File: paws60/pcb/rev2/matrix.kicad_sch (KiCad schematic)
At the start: 139 parts

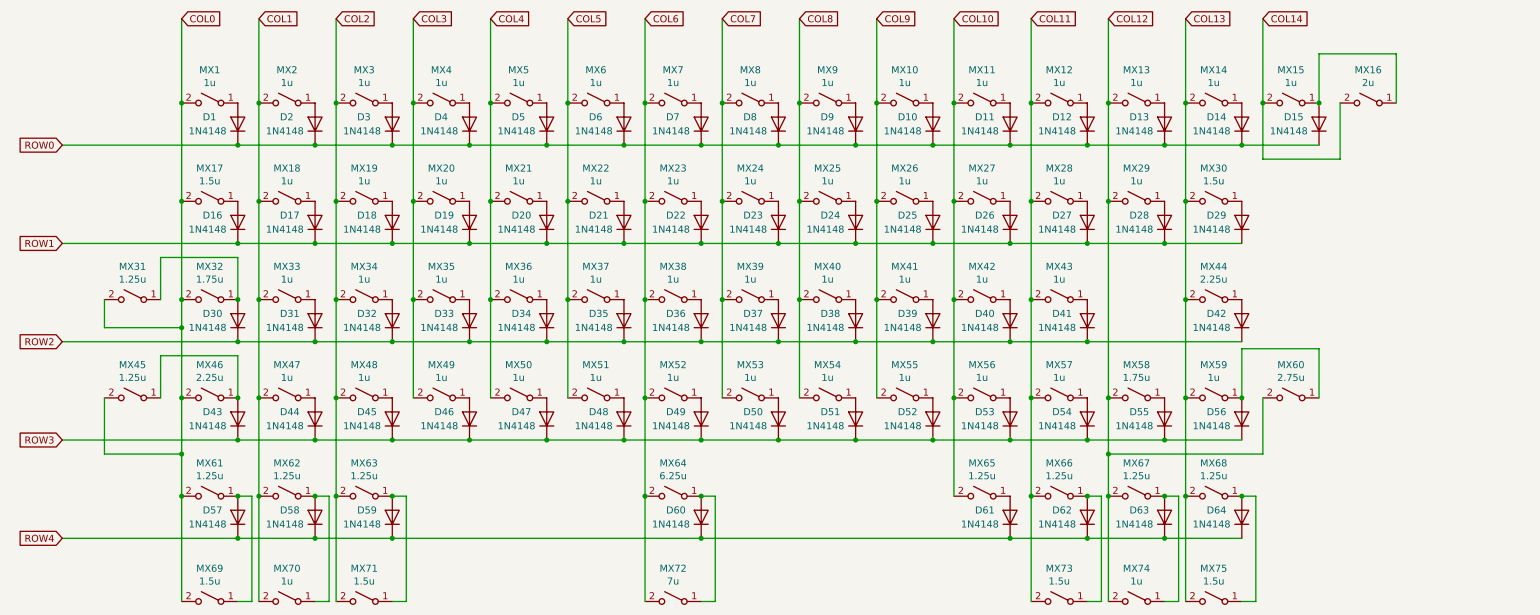
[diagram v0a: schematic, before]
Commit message: Update paws60 hotswap socket footprint and lazulipad
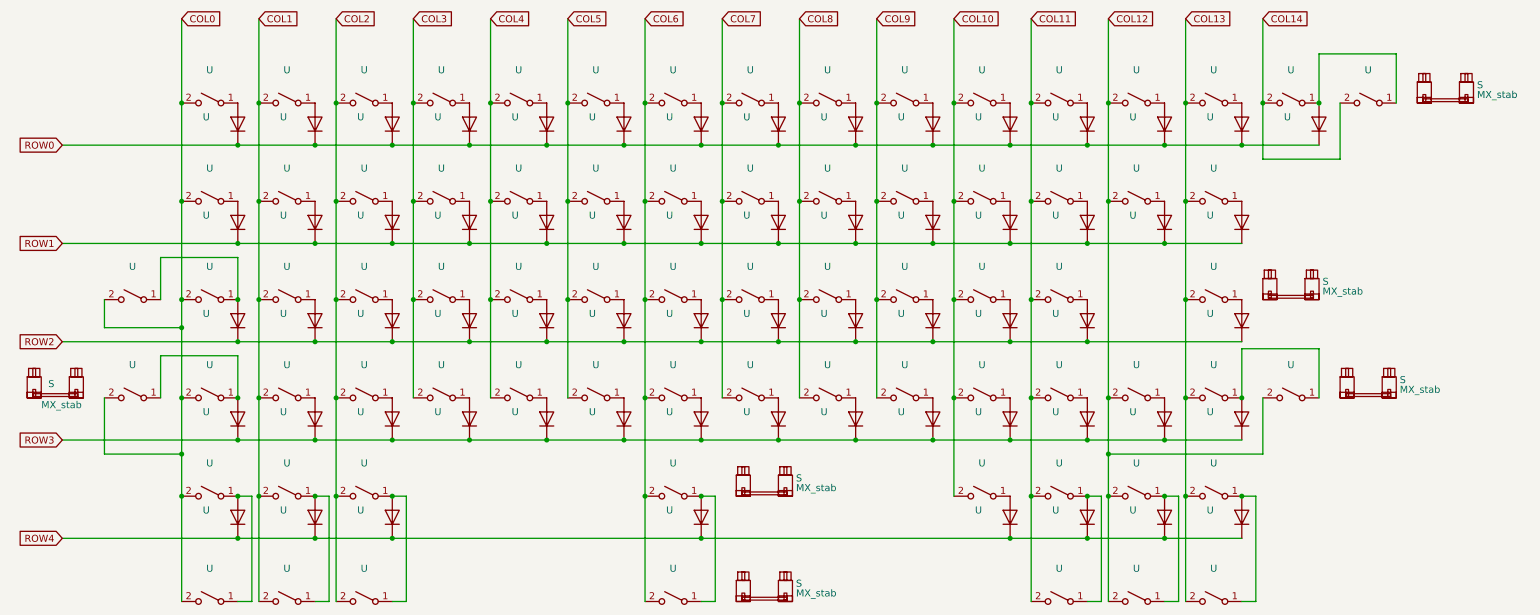
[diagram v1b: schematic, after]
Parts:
- added S (x6): MX_stab, marbastlib-mx:STAB_MX_P_6.25u, symbol marbastlib-mx:MX_stab
- U: renamed from MX60; value 2.75u -> (none); footprint MX_Only:MXOnly-2.75U-Hotswap -> (none)
- U: renamed from MX74; value 1u -> (none); footprint MX_Only:MXOnly-1U-Hotswap -> (none)
- U: renamed from MX75; value 1.5u -> (none); footprint MX_Only:MXOnly-1.5U-Hotswap -> (none)
- U: renamed from MX72; value 7u -> (none); footprint MX_Only:MXOnly-7U-Hotswap -> (none)
- U: renamed from MX69; value 1.5u -> (none); footprint MX_Only:MXOnly-1.5U-Hotswap -> (none)
- U: renamed from MX70; value 1u -> (none); footprint MX_Only:MXOnly-1U-Hotswap -> (none)
- U: renamed from MX71; value 1.5u -> (none); footprint MX_Only:MXOnly-1.5U-Hotswap -> (none)
- U: renamed from MX17; value 1.5u -> (none); footprint MX_Only:MXOnly-1.5U-Hotswap -> (none)
- U: renamed from MX5; value 1u -> (none); footprint MX_Only:MXOnly-1U-Hotswap -> (none)
- U: renamed from MX31; value 1.25u -> (none); footprint MX_Only:MXOnly-1.25U-Hotswap -> (none)
- U: renamed from MX16; value 2u -> (none); footprint MX_Only:MXOnly-2U-Hotswap -> (none)
- U: renamed from MX73; value 1.5u -> (none); footprint MX_Only:MXOnly-1.5U-Hotswap -> (none)
- U: renamed from MX32; value 1.75u -> (none); footprint MX_Only:MXOnly-1.75U-Hotswap -> (none)
- U: renamed from MX46; value 2.25u -> (none); footprint MX_Only:MXOnly-2.25U-Hotswap -> (none)
- U: renamed from D64; value 1N4148 -> (none); footprint Diode_SMD:D_SOD-123 -> (none)
- U: renamed from MX68; value 1.25u -> (none); footprint MX_Only:MXOnly-1.25U-Hotswap -> (none)
- U: renamed from D63; value 1N4148 -> (none); footprint Diode_SMD:D_SOD-123 -> (none)
- U: renamed from MX67; value 1.25u -> (none); footprint MX_Only:MXOnly-1.25U-Hotswap -> (none)
- U: renamed from D62; value 1N4148 -> (none); footprint Diode_SMD:D_SOD-123 -> (none)
- U: renamed from MX66; value 1.25u -> (none); footprint MX_Only:MXOnly-1.25U-Hotswap -> (none)
- U: renamed from D61; value 1N4148 -> (none); footprint Diode_SMD:D_SOD-123 -> (none)
- U: renamed from MX65; value 1.25u -> (none); footprint MX_Only:MXOnly-1.25U-Hotswap -> (none)
- U: renamed from D60; value 1N4148 -> (none); footprint Diode_SMD:D_SOD-123 -> (none)
- U: renamed from MX64; value 6.25u -> (none); footprint MX_Only:MXOnly-6.25U-Hotswap-ReversedStabilizers -> (none)
- U: renamed from D59; value 1N4148 -> (none); footprint Diode_SMD:D_SOD-123 -> (none)
- U: renamed from MX63; value 1.25u -> (none); footprint MX_Only:MXOnly-1.25U-Hotswap -> (none)
- U: renamed from D58; value 1N4148 -> (none); footprint Diode_SMD:D_SOD-123 -> (none)
- U: renamed from MX62; value 1.25u -> (none); footprint MX_Only:MXOnly-1.25U-Hotswap -> (none)
- U: renamed from D57; value 1N4148 -> (none); footprint Diode_SMD:D_SOD-123 -> (none)
- U: renamed from MX61; value 1.25u -> (none); footprint MX_Only:MXOnly-1.25U-Hotswap -> (none)
- U: renamed from D56; value 1N4148 -> (none); footprint Diode_SMD:D_SOD-123 -> (none)
- U: renamed from MX59; value 1u -> (none); footprint MX_Only:MXOnly-1U-Hotswap -> (none)
- U: renamed from D55; value 1N4148 -> (none); footprint Diode_SMD:D_SOD-123 -> (none)
- U: renamed from MX58; value 1.75u -> (none); footprint MX_Only:MXOnly-1.75U-Hotswap -> (none)
- U: renamed from D54; value 1N4148 -> (none); footprint Diode_SMD:D_SOD-123 -> (none)
- U: renamed from MX57; value 1u -> (none); footprint MX_Only:MXOnly-1U-Hotswap -> (none)
- U: renamed from D53; value 1N4148 -> (none); footprint Diode_SMD:D_SOD-123 -> (none)
- U: renamed from MX56; value 1u -> (none); footprint MX_Only:MXOnly-1U-Hotswap -> (none)
- U: renamed from D52; value 1N4148 -> (none); footprint Diode_SMD:D_SOD-123 -> (none)
- U: renamed from MX55; value 1u -> (none); footprint MX_Only:MXOnly-1U-Hotswap -> (none)
- U: renamed from D51; value 1N4148 -> (none); footprint Diode_SMD:D_SOD-123 -> (none)
- U: renamed from MX54; value 1u -> (none); footprint MX_Only:MXOnly-1U-Hotswap -> (none)
- U: renamed from D50; value 1N4148 -> (none); footprint Diode_SMD:D_SOD-123 -> (none)
- U: renamed from MX53; value 1u -> (none); footprint MX_Only:MXOnly-1U-Hotswap -> (none)
- U: renamed from D49; value 1N4148 -> (none); footprint Diode_SMD:D_SOD-123 -> (none)
- U: renamed from MX52; value 1u -> (none); footprint MX_Only:MXOnly-1U-Hotswap -> (none)
- U: renamed from D48; value 1N4148 -> (none); footprint Diode_SMD:D_SOD-123 -> (none)
- U: renamed from MX51; value 1u -> (none); footprint MX_Only:MXOnly-1U-Hotswap -> (none)
- U: renamed from D47; value 1N4148 -> (none); footprint Diode_SMD:D_SOD-123 -> (none)
- U: renamed from MX50; value 1u -> (none); footprint MX_Only:MXOnly-1U-Hotswap -> (none)
- U: renamed from D46; value 1N4148 -> (none); footprint Diode_SMD:D_SOD-123 -> (none)
- U: renamed from MX49; value 1u -> (none); footprint MX_Only:MXOnly-1U-Hotswap -> (none)
- U: renamed from D45; value 1N4148 -> (none); footprint Diode_SMD:D_SOD-123 -> (none)
- U: renamed from MX48; value 1u -> (none); footprint MX_Only:MXOnly-1U-Hotswap -> (none)
- U: renamed from D43; value 1N4148 -> (none); footprint Diode_SMD:D_SOD-123 -> (none)
- U: renamed from D42; value 1N4148 -> (none); footprint Diode_SMD:D_SOD-123 -> (none)
- U: renamed from MX44; value 2.25u -> (none); footprint MX_Only:MXOnly-2.25U-Hotswap -> (none)
- U: renamed from D41; value 1N4148 -> (none); footprint Diode_SMD:D_SOD-123 -> (none)
- U: renamed from MX43; value 1u -> (none); footprint MX_Only:MXOnly-1U-Hotswap -> (none)
- U: renamed from D40; value 1N4148 -> (none); footprint Diode_SMD:D_SOD-123 -> (none)
- U: renamed from MX42; value 1u -> (none); footprint MX_Only:MXOnly-1U-Hotswap -> (none)
- U: renamed from D39; value 1N4148 -> (none); footprint Diode_SMD:D_SOD-123 -> (none)
- U: renamed from MX41; value 1u -> (none); footprint MX_Only:MXOnly-1U-Hotswap -> (none)
- U: renamed from D38; value 1N4148 -> (none); footprint Diode_SMD:D_SOD-123 -> (none)
- U: renamed from MX40; value 1u -> (none); footprint MX_Only:MXOnly-1U-Hotswap -> (none)
- U: renamed from D37; value 1N4148 -> (none); footprint Diode_SMD:D_SOD-123 -> (none)
- U: renamed from MX39; value 1u -> (none); footprint MX_Only:MXOnly-1U-Hotswap -> (none)
- U: renamed from D36; value 1N4148 -> (none); footprint Diode_SMD:D_SOD-123 -> (none)
- U: renamed from MX38; value 1u -> (none); footprint MX_Only:MXOnly-1U-Hotswap -> (none)
- U: renamed from D35; value 1N4148 -> (none); footprint Diode_SMD:D_SOD-123 -> (none)
- U: renamed from MX37; value 1u -> (none); footprint MX_Only:MXOnly-1U-Hotswap -> (none)
- U: renamed from D34; value 1N4148 -> (none); footprint Diode_SMD:D_SOD-123 -> (none)
- U: renamed from MX36; value 1u -> (none); footprint MX_Only:MXOnly-1U-Hotswap -> (none)
- U: renamed from D33; value 1N4148 -> (none); footprint Diode_SMD:D_SOD-123 -> (none)
- U: renamed from MX35; value 1u -> (none); footprint MX_Only:MXOnly-1U-Hotswap -> (none)
- U: renamed from D32; value 1N4148 -> (none); footprint Diode_SMD:D_SOD-123 -> (none)
- U: renamed from MX34; value 1u -> (none); footprint MX_Only:MXOnly-1U-Hotswap -> (none)
- U: renamed from D31; value 1N4148 -> (none); footprint Diode_SMD:D_SOD-123 -> (none)
- U: renamed from MX33; value 1u -> (none); footprint MX_Only:MXOnly-1U-Hotswap -> (none)
- U: renamed from D30; value 1N4148 -> (none); footprint Diode_SMD:D_SOD-123 -> (none)
- U: renamed from D29; value 1N4148 -> (none); footprint Diode_SMD:D_SOD-123 -> (none)
- U: renamed from MX30; value 1.5u -> (none); footprint MX_Only:MXOnly-1.5U-Hotswap -> (none)
- U: renamed from D28; value 1N4148 -> (none); footprint Diode_SMD:D_SOD-123 -> (none)
- U: renamed from MX29; value 1u -> (none); footprint MX_Only:MXOnly-1U-Hotswap -> (none)
- U: renamed from D27; value 1N4148 -> (none); footprint Diode_SMD:D_SOD-123 -> (none)
- U: renamed from MX28; value 1u -> (none); footprint MX_Only:MXOnly-1U-Hotswap -> (none)
- U: renamed from D26; value 1N4148 -> (none); footprint Diode_SMD:D_SOD-123 -> (none)
- U: renamed from MX27; value 1u -> (none); footprint MX_Only:MXOnly-1U-Hotswap -> (none)
- U: renamed from D25; value 1N4148 -> (none); footprint Diode_SMD:D_SOD-123 -> (none)
- U: renamed from MX26; value 1u -> (none); footprint MX_Only:MXOnly-1U-Hotswap -> (none)
- U: renamed from D24; value 1N4148 -> (none); footprint Diode_SMD:D_SOD-123 -> (none)
- U: renamed from MX25; value 1u -> (none); footprint MX_Only:MXOnly-1U-Hotswap -> (none)
- U: renamed from D23; value 1N4148 -> (none); footprint Diode_SMD:D_SOD-123 -> (none)
- U: renamed from MX24; value 1u -> (none); footprint MX_Only:MXOnly-1U-Hotswap -> (none)
- U: renamed from D22; value 1N4148 -> (none); footprint Diode_SMD:D_SOD-123 -> (none)
- U: renamed from MX23; value 1u -> (none); footprint MX_Only:MXOnly-1U-Hotswap -> (none)
- U: renamed from D21; value 1N4148 -> (none); footprint Diode_SMD:D_SOD-123 -> (none)
- U: renamed from MX22; value 1u -> (none); footprint MX_Only:MXOnly-1U-Hotswap -> (none)
- U: renamed from D20; value 1N4148 -> (none); footprint Diode_SMD:D_SOD-123 -> (none)
- U: renamed from MX21; value 1u -> (none); footprint MX_Only:MXOnly-1U-Hotswap -> (none)
- U: renamed from D19; value 1N4148 -> (none); footprint Diode_SMD:D_SOD-123 -> (none)
- U: renamed from MX20; value 1u -> (none); footprint MX_Only:MXOnly-1U-Hotswap -> (none)
- U: renamed from D18; value 1N4148 -> (none); footprint Diode_SMD:D_SOD-123 -> (none)
- U: renamed from MX19; value 1u -> (none); footprint MX_Only:MXOnly-1U-Hotswap -> (none)
- U: renamed from D17; value 1N4148 -> (none); footprint Diode_SMD:D_SOD-123 -> (none)
- U: renamed from MX18; value 1u -> (none); footprint MX_Only:MXOnly-1U-Hotswap -> (none)
- U: renamed from D16; value 1N4148 -> (none); footprint Diode_SMD:D_SOD-123 -> (none)
- U: renamed from D15; value 1N4148 -> (none); footprint Diode_SMD:D_SOD-123 -> (none)
- U: renamed from MX15; value 1u -> (none); footprint MX_Only:MXOnly-1U-Hotswap -> (none)
- U: renamed from D14; value 1N4148 -> (none); footprint Diode_SMD:D_SOD-123 -> (none)
- U: renamed from MX14; value 1u -> (none); footprint MX_Only:MXOnly-1U-Hotswap -> (none)
- U: renamed from D13; value 1N4148 -> (none); footprint Diode_SMD:D_SOD-123 -> (none)
- U: renamed from MX13; value 1u -> (none); footprint MX_Only:MXOnly-1U-Hotswap -> (none)
- U: renamed from D12; value 1N4148 -> (none); footprint Diode_SMD:D_SOD-123 -> (none)
- U: renamed from MX12; value 1u -> (none); footprint MX_Only:MXOnly-1U-Hotswap -> (none)
- U: renamed from D11; value 1N4148 -> (none); footprint Diode_SMD:D_SOD-123 -> (none)
- U: renamed from MX11; value 1u -> (none); footprint MX_Only:MXOnly-1U-Hotswap -> (none)
- U: renamed from D10; value 1N4148 -> (none); footprint Diode_SMD:D_SOD-123 -> (none)
- U: renamed from MX10; value 1u -> (none); footprint MX_Only:MXOnly-1U-Hotswap -> (none)
- U: renamed from D9; value 1N4148 -> (none); footprint Diode_SMD:D_SOD-123 -> (none)
- U: renamed from MX9; value 1u -> (none); footprint MX_Only:MXOnly-1U-Hotswap -> (none)
- U: renamed from D8; value 1N4148 -> (none); footprint Diode_SMD:D_SOD-123 -> (none)
- U: renamed from MX8; value 1u -> (none); footprint MX_Only:MXOnly-1U-Hotswap -> (none)
- U: renamed from D7; value 1N4148 -> (none); footprint Diode_SMD:D_SOD-123 -> (none)
- U: renamed from MX7; value 1u -> (none); footprint MX_Only:MXOnly-1U-Hotswap -> (none)
- U: renamed from D6; value 1N4148 -> (none); footprint Diode_SMD:D_SOD-123 -> (none)
- U: renamed from MX6; value 1u -> (none); footprint MX_Only:MXOnly-1U-Hotswap -> (none)
- U: renamed from D5; value 1N4148 -> (none); footprint Diode_SMD:D_SOD-123 -> (none)
- U: renamed from D4; value 1N4148 -> (none); footprint Diode_SMD:D_SOD-123 -> (none)
- U: renamed from MX4; value 1u -> (none); footprint MX_Only:MXOnly-1U-Hotswap -> (none)
- U: renamed from D3; value 1N4148 -> (none); footprint Diode_SMD:D_SOD-123 -> (none)
- U: renamed from MX3; value 1u -> (none); footprint MX_Only:MXOnly-1U-Hotswap -> (none)
- U: renamed from D2; value 1N4148 -> (none); footprint Diode_SMD:D_SOD-123 -> (none)
- U: renamed from MX2; value 1u -> (none); footprint MX_Only:MXOnly-1U-Hotswap -> (none)
- U: renamed from D1; value 1N4148 -> (none); footprint Diode_SMD:D_SOD-123 -> (none)
- U: renamed from MX1; value 1u -> (none); footprint MX_Only:MXOnly-1U-Hotswap -> (none)
- U: renamed from MX47; value 1u -> (none); footprint MX_Only:MXOnly-1U-Hotswap -> (none)
- U: renamed from D44; value 1N4148 -> (none); footprint Diode_SMD:D_SOD-123 -> (none)
- U: renamed from MX45; value 1.25u -> (none); footprint MX_Only:MXOnly-1.25U-Hotswap -> (none)
